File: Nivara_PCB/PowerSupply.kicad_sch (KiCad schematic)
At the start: 19 parts, among them U2 AP63200WU

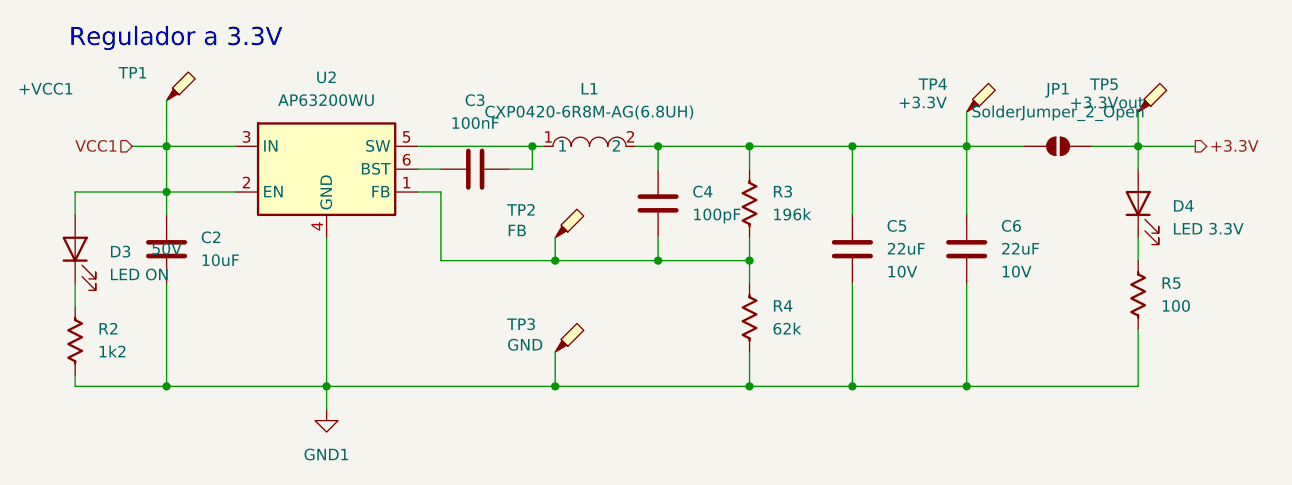
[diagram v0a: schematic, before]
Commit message: Cambios en el PCB de Nivara. Ruteo de emtradas y salidas NPN y PNP.
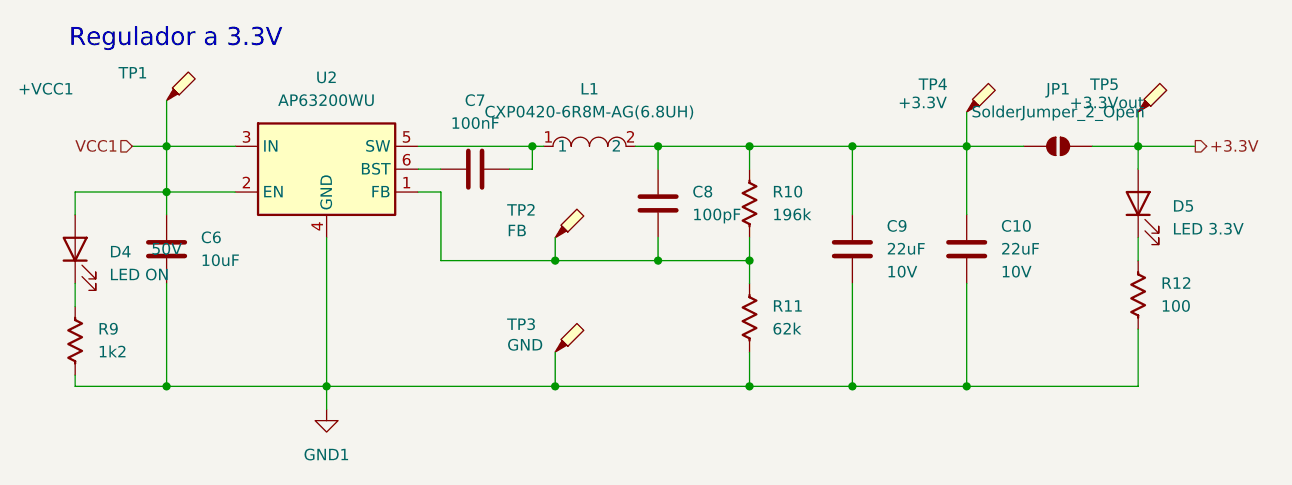
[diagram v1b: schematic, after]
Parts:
- renumbered C6 to C10, C2 to C6, C3 to C7, C4 to C8, C5 to C9, D3 to D4, D4 to D5, R3 to R10, R4 to R11, R5 to R12, R2 to R9
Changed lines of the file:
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@@
 		(dnp no)
 		(fields_autoplaced yes)
-		(property "Reference" "R5"
+		(property "Reference" "R12"
 			(at 163.83 62.2299 0)
 			(effects
@@
 			(project "Nivara_PCB"
 				(path "/13184db0-a71d-4054-b13a-bbf46d2b100d/4e7fa7f2-8bf5-4f9c-874d-fa1b4fd76f92/c8cd749e-9134-4d76-b8ef-ce0eb3eb606f"
-					(reference "R5")
+					(reference "R12")
 					(unit 1)
 				)
@@
 		(dnp no)
 		(fields_autoplaced yes)
-		(property "Reference" "C2"
+		(property "Reference" "C6"
 			(at 57.15 57.1499 0)
 			(effects
@@
 			(project ""
 				(path "/13184db0-a71d-4054-b13a-bbf46d2b100d/4e7fa7f2-8bf5-4f9c-874d-fa1b4fd76f92/c8cd749e-9134-4d76-b8ef-ce0eb3eb606f"
-					(reference "C2")
+					(reference "C6")
 					(unit 1)
 				)
@@
 		(dnp no)
 		(fields_autoplaced yes)
-		(property "Reference" "R2"
+		(property "Reference" "R9"
 			(at 45.72 67.3099 0)
 			(effects
@@
 			(project "Nivara_PCB"
 				(path "/13184db0-a71d-4054-b13a-bbf46d2b100d/4e7fa7f2-8bf5-4f9c-874d-fa1b4fd76f92/c8cd749e-9134-4d76-b8ef-ce0eb3eb606f"
-					(reference "R2")
+					(reference "R9")
 					(unit 1)
 				)
@@
 		(dnp no)
 		(fields_autoplaced yes)
-		(property "Reference" "D3"
+		(property "Reference" "D4"
 			(at 46.99 58.7374 90)
 			(effects
@@
 			(project ""
 				(path "/13184db0-a71d-4054-b13a-bbf46d2b100d/4e7fa7f2-8bf5-4f9c-874d-fa1b4fd76f92/c8cd749e-9134-4d76-b8ef-ce0eb3eb606f"
-					(reference "D3")
+					(reference "D4")
 					(unit 1)
 				)
@@
 		(dnp no)
 		(fields_autoplaced yes)
-		(property "Reference" "C6"
+		(property "Reference" "C10"
 			(at 146.05 55.8799 0)
 			(effects
@@
 			(project "Nivara_PCB"
 				(path "/13184db0-a71d-4054-b13a-bbf46d2b100d/4e7fa7f2-8bf5-4f9c-874d-fa1b4fd76f92/c8cd749e-9134-4d76-b8ef-ce0eb3eb606f"
-					(reference "C6")
+					(reference "C10")
 					(unit 1)
 				)
@@
 		(dnp no)
 		(fields_autoplaced yes)
-		(property "Reference" "#PWR023"
+		(property "Reference" "#PWR044"
 			(at 71.12 82.55 0)
 			(effects
@@
 			(project "Nivara_PCB"
 				(path "/13184db0-a71d-4054-b13a-bbf46d2b100d/4e7fa7f2-8bf5-4f9c-874d-fa1b4fd76f92/c8cd749e-9134-4d76-b8ef-ce0eb3eb606f"
-					(reference "#PWR023")
+					(reference "#PWR044")
 					(unit 1)
 				)
@@
 		(dnp no)
 		(fields_autoplaced yes)
-		(property "Reference" "R3"
+		(property "Reference" "R10"
 			(at 120.65 52.0699 0)
 			(effects
@@
 			(project ""
 				(path "/13184db0-a71d-4054-b13a-bbf46d2b100d/4e7fa7f2-8bf5-4f9c-874d-fa1b4fd76f92/c8cd749e-9134-4d76-b8ef-ce0eb3eb606f"
-					(reference "R3")
+					(reference "R10")
 					(unit 1)
 				)
@@
 		(dnp no)
 		(fields_autoplaced yes)
-		(property "Reference" "C5"
+		(property "Reference" "C9"
 			(at 133.35 55.8799 0)
 			(effects
@@
 			(project "Nivara_PCB"
 				(path "/13184db0-a71d-4054-b13a-bbf46d2b100d/4e7fa7f2-8bf5-4f9c-874d-fa1b4fd76f92/c8cd749e-9134-4d76-b8ef-ce0eb3eb606f"
-					(reference "C5")
+					(reference "C9")
 					(unit 1)
 				)
@@
 		(dnp no)
 		(fields_autoplaced yes)
-		(property "Reference" "D4"
+		(property "Reference" "D5"
 			(at 165.1 53.6574 90)
 			(effects
@@
 			(project "Nivara_PCB"
 				(path "/13184db0-a71d-4054-b13a-bbf46d2b100d/4e7fa7f2-8bf5-4f9c-874d-fa1b4fd76f92/c8cd749e-9134-4d76-b8ef-ce0eb3eb606f"
-					(reference "D4")
+					(reference "D5")
 					(unit 1)
 				)
@@
 		(dnp no)
 		(fields_autoplaced yes)
-		(property "Reference" "R4"
+		(property "Reference" "R11"
 			(at 120.65 64.7699 0)
 			(effects
@@
 			(project "Nivara_PCB"
 				(path "/13184db0-a71d-4054-b13a-bbf46d2b100d/4e7fa7f2-8bf5-4f9c-874d-fa1b4fd76f92/c8cd749e-9134-4d76-b8ef-ce0eb3eb606f"
-					(reference "R4")
+					(reference "R11")
 					(unit 1)
 				)
@@
 		(dnp no)
 		(fields_autoplaced yes)
-		(property "Reference" "C3"
+		(property "Reference" "C7"
 			(at 87.63 41.91 90)
 			(effects
@@
 			(project "Nivara_PCB"
 				(path "/13184db0-a71d-4054-b13a-bbf46d2b100d/4e7fa7f2-8bf5-4f9c-874d-fa1b4fd76f92/c8cd749e-9134-4d76-b8ef-ce0eb3eb606f"
-					(reference "C3")
+					(reference "C7")
 					(unit 1)
 				)
@@
 		(dnp no)
 		(fields_autoplaced yes)
-		(property "Reference" "C4"
+		(property "Reference" "C8"
 			(at 111.76 52.0699 0)
 			(effects
@@
 			(project "Nivara_PCB"
 				(path "/13184db0-a71d-4054-b13a-bbf46d2b100d/4e7fa7f2-8bf5-4f9c-874d-fa1b4fd76f92/c8cd749e-9134-4d76-b8ef-ce0eb3eb606f"
-					(reference "C4")
-					(unit 1)
-				)
+					(reference "C8")
+					(unit 1)
+				)
